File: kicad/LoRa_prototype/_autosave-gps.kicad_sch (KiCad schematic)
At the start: 15 parts, among them Q1 DTC143Z, Q2 DTC143Z, U6 L80-R

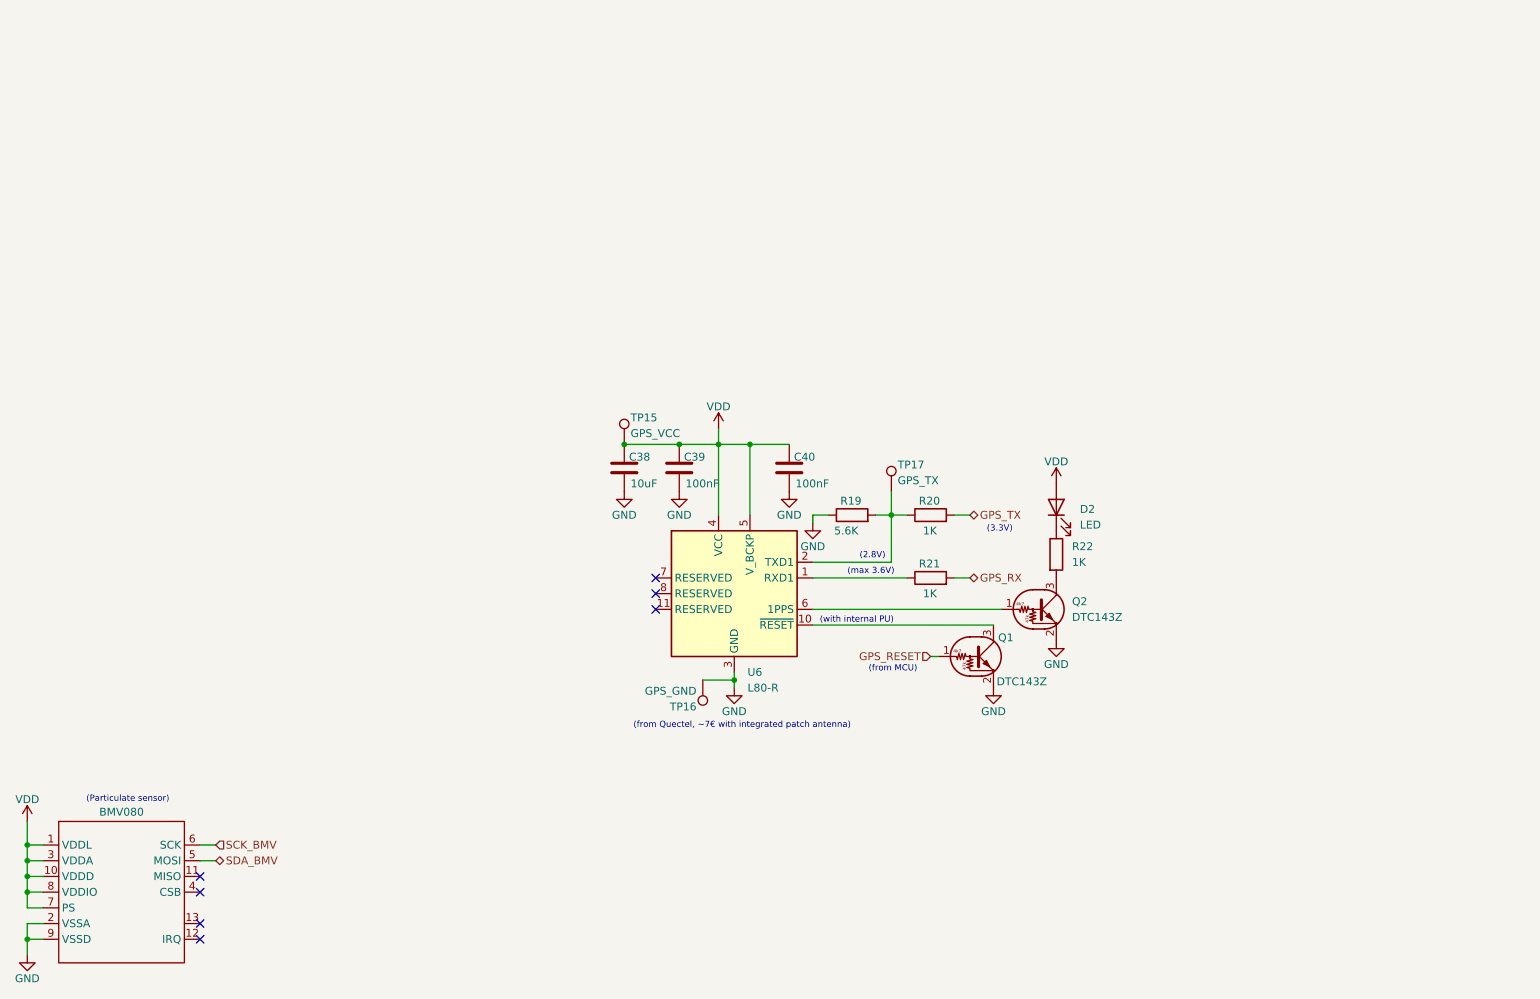
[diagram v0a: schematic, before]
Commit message: Started adding gas sensors to schematic
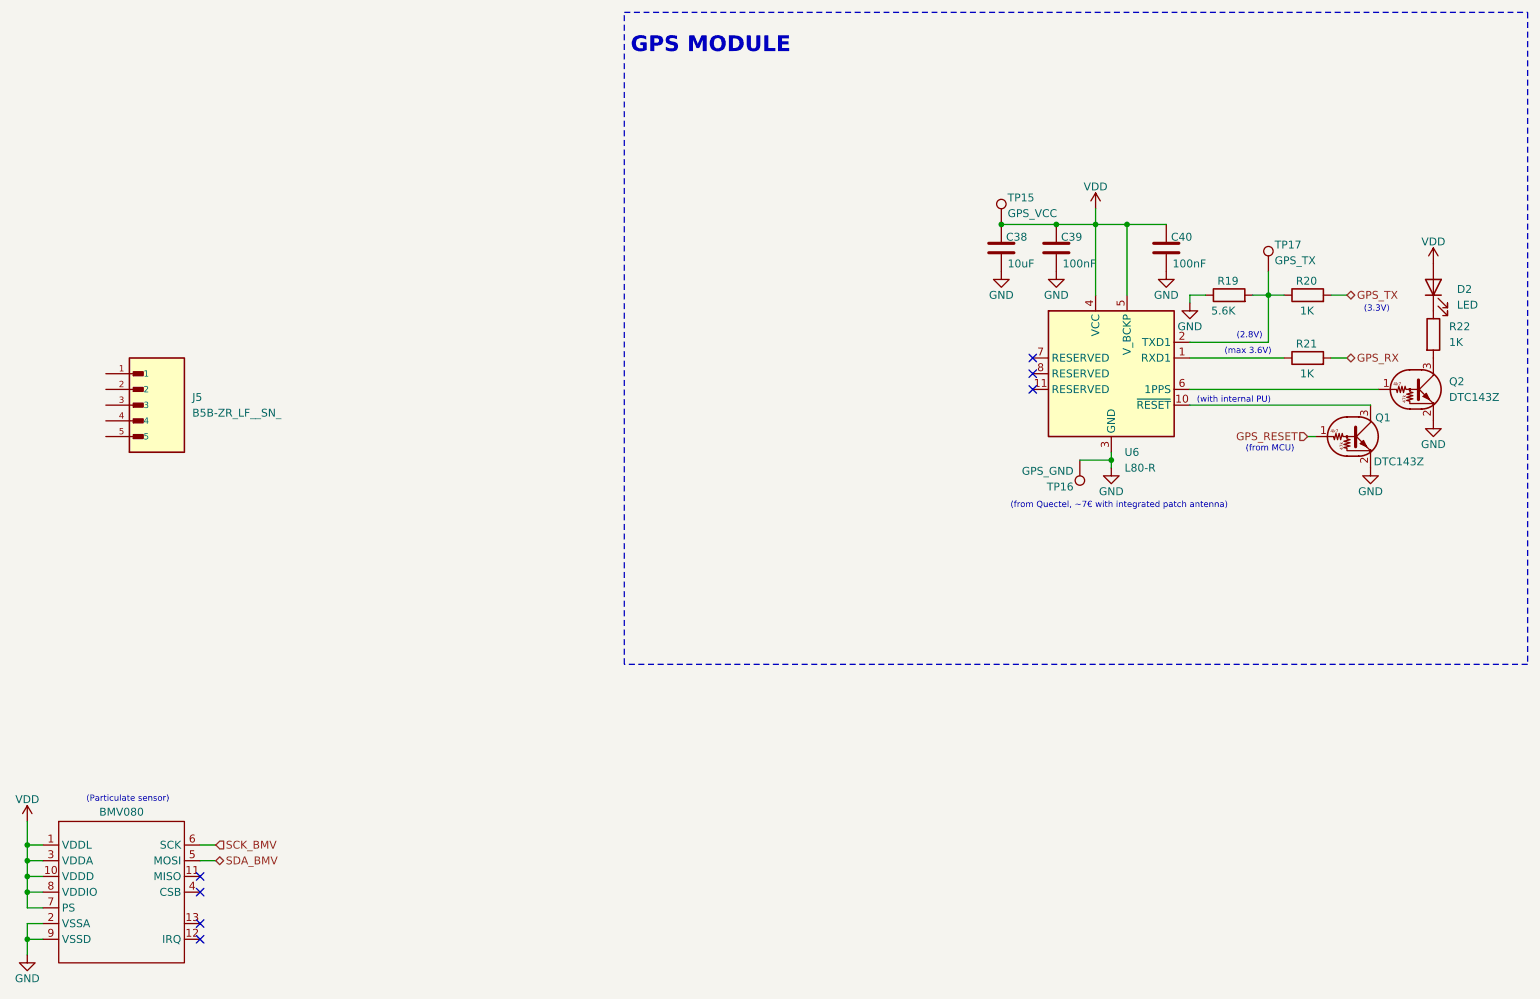
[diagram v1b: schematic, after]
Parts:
- added J5: B5B-ZR_LF__SN_, B5B-ZR_LF__SN_:JST_B5B-ZR_LF__SN_, symbol B5B-ZR_LF__SN_:B5B-ZR_LF__SN_
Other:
- note added: "GPS MODULE"
- moved on the sheet: C38, C39, C40, D2, Q1, Q2, R19, R20, R21, R22, TP15, TP16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
